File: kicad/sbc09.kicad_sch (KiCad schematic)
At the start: 77 parts, among them J1 Conn_01x03_Male, J2 Conn_01x06_Male, J3 Conn_01x06_Male, J4 Conn_01x06_Male, J5 DB9_Female_MountingHoles, J6 Conn_02x25_Odd_Even, Q1 2N7000, SW1 SW_Push, U1 74LS245, U10 74LS670, U11 74LS670, U12 AS6C4008-55PCN, U13 SST39SF040-DIP, U14 SST39SF040-DIP, U15 XR68C681CJ, U16 MAX232, U2 74LS245, U3 74LS245, U4 MC6809E, U5 74HCT125, U6 ATF22V10C, U7 ATF22V10C, U8 74LS670, U9 74LS670, X1 8MHz, X2 3.6864MHz

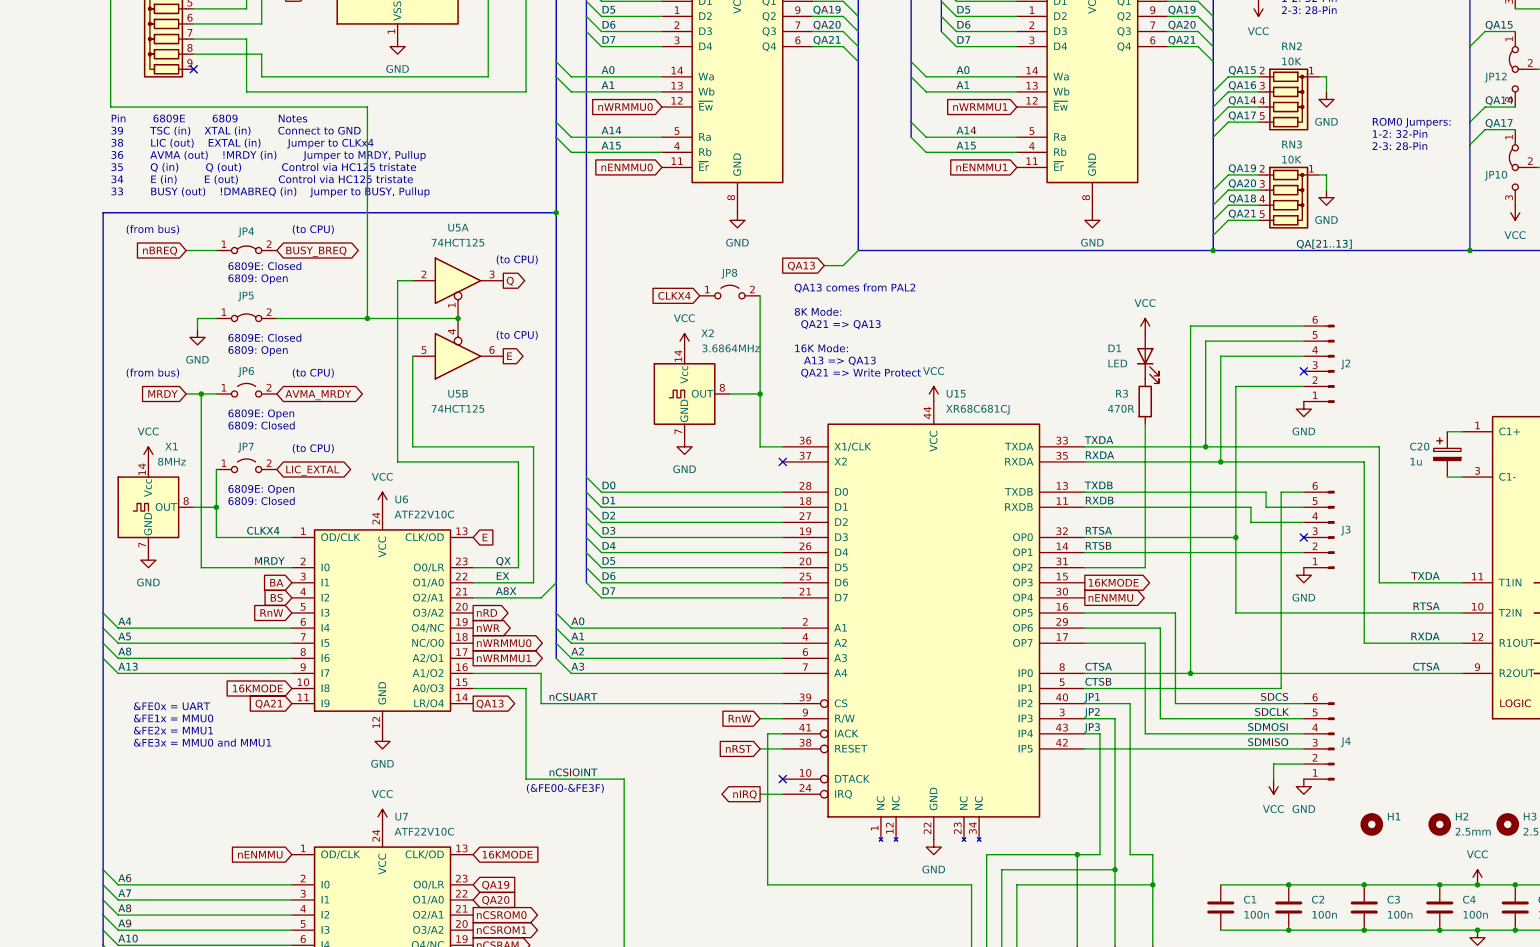
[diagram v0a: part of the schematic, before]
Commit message: Tweak board placement; DIP-8 oscillators
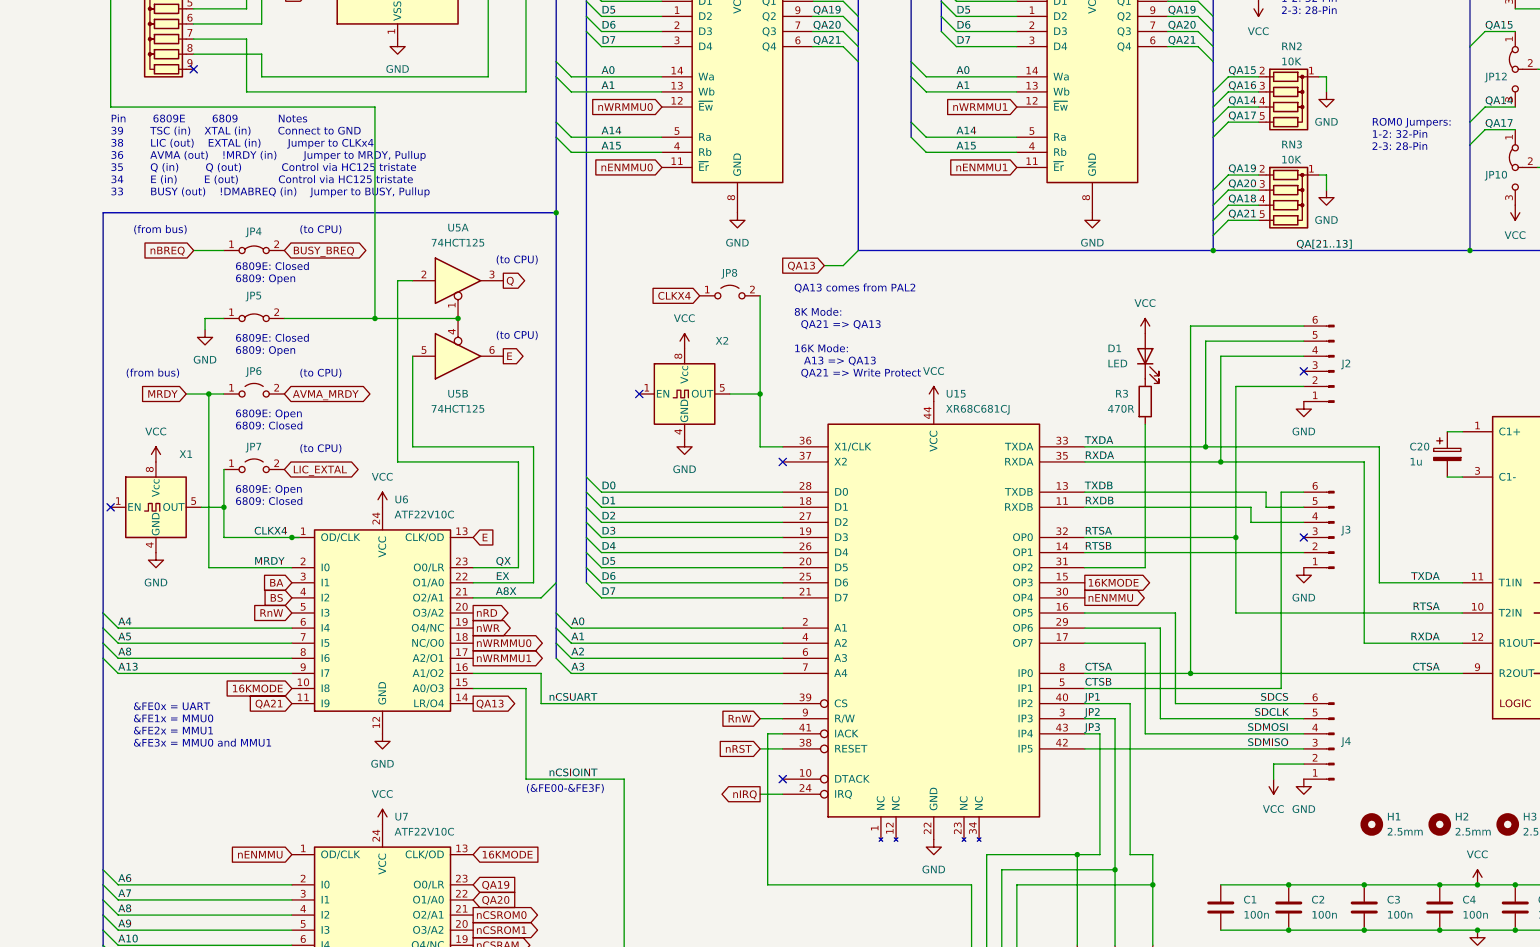
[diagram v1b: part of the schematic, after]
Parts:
- removed X1: 8MHz, Oscillator:Oscillator_DIP-14, symbol Oscillator:ACO-xxxMHz
- removed X2: 3.6864MHz, Oscillator:Oscillator_DIP-14, symbol Oscillator:ACO-xxxMHz
- added X1: (no value), symbol Oscillator:CXO_DIP8
- added X2: (no value), Oscillator:Oscillator_DIP-8, symbol Oscillator:CXO_DIP8
- H1: value (none) -> 2.5mm
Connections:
- net CLKX4: now also X1.5 (OUT)
- net GND: now also X1.4 (GND), X2.4 (GND)
- net VCC: now also X1.8 (Vcc), X2.8 (Vcc)
- net at JP8.2 (B), U15.36 (X1/CLK): now also X2.5 (OUT)
- no-connect marks 14 -> 16
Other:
- moved on the sheet: JP4, JP5, JP6, JP7

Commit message: Minor
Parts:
- J2, J3: footprint Connector_PinSocket_2.54mm:PinSocket_1x06_P2.54mm_Vertical -> (none)
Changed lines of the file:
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@@
       (effects (font (size 1.27 1.27)) (justify right) hide)
     )
-    (property "Footprint" "Connector_PinSocket_2.54mm:PinSocket_1x06_P2.54mm_Vertical" (id 2) (at 222.25 190.5 0)
+    (property "Footprint" "" (id 2) (at 222.25 190.5 0)
       (effects (font (size 1.27 1.27)) hide)
     )
@@
       (effects (font (size 1.27 1.27)) (justify right) hide)
     )
-    (property "Footprint" "Connector_PinSocket_2.54mm:PinSocket_1x06_P2.54mm_Vertical" (id 2) (at 222.25 162.56 0)
-      (effects (font (size 1.27 1.27)) hide)
-    )
+    (property "Footprint" "" (id 2) (at 222.25 162.56 0)
+      (effects (font (size 1.27 1.27)) hide)
+    )

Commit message: Messing with front panel connectors
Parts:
- D1: footprint LED_THT:LED_D3.0mm -> (none)
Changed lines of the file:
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@@
       (effects (font (size 1.27 1.27)) (justify right))
     )
-    (property "Footprint" "LED_THT:LED_D3.0mm" (id 2) (at 190.5 160.02 0)
+    (property "Footprint" "" (id 2) (at 190.5 160.02 0)
       (effects (font (size 1.27 1.27)) hide)
     )
@@
     )
     (path "/fae83aca-d871-4dad-8dca-794c894d9124"
-      (reference "D1") (unit 1) (value "LED") (footprint "LED_THT:LED_D3.0mm")
+      (reference "D1") (unit 1) (value "LED") (footprint "LED_THT:LED_D3.0mm_Horizontal_O1.27mm_Z2.0mm")
     )
     (path "/0fdc7ebb-4b15-4947-a92f-73b17a1787e1"
@@
     )
     (path "/c8679364-5ecf-4ff5-92b0-70a3c93f3773"
-      (reference "J2") (unit 1) (value "Conn_01x06_Male") (footprint "Connector_PinSocket_2.54mm:PinSocket_1x06_P2.54mm_Vertical")
+      (reference "J2") (unit 1) (value "Conn_01x06_Male") (footprint "Connector_PinSocket_2.54mm:PinSocket_1x06_P2.54mm_Horizontal")
     )
     (path "/04d3812c-7a47-4d20-b313-0d4dd0f3856c"
-      (reference "J3") (unit 1) (value "Conn_01x06_Male") (footprint "Connector_PinSocket_2.54mm:PinSocket_1x06_P2.54mm_Vertical")
+      (reference "J3") (unit 1) (value "Conn_01x06_Male") (footprint "Connector_PinSocket_2.54mm:PinSocket_1x06_P2.54mm_Horizontal")
     )
     (path "/acbf984b-95e6-48f0-909b-46f570b1f9ff"

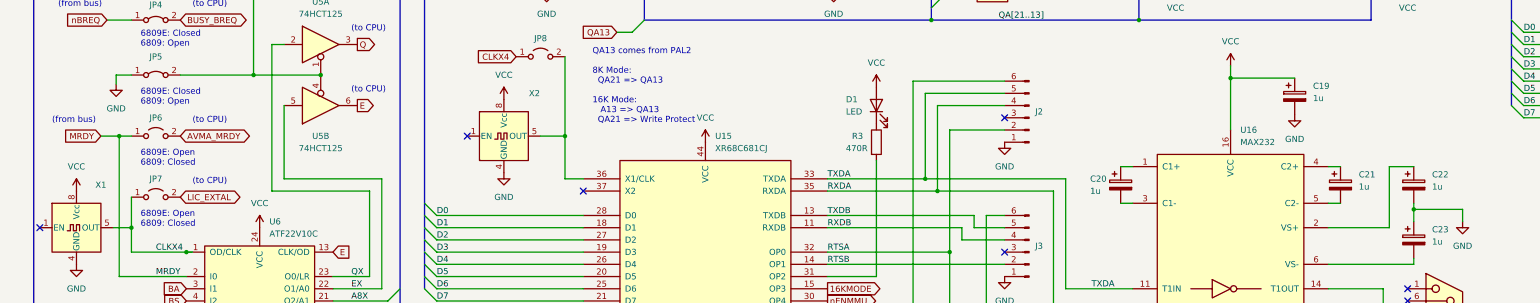
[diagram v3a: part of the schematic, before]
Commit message: OCD tweaking around MAX232E
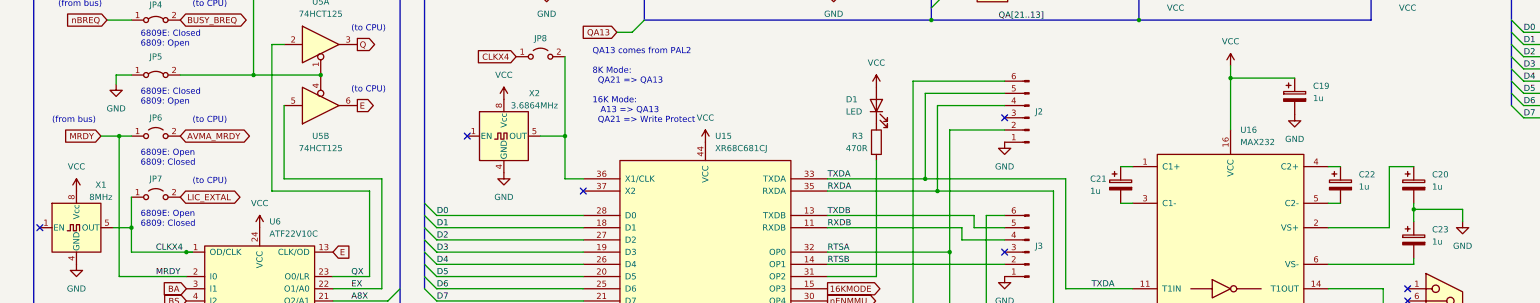
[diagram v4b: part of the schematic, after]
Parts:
- D1: footprint (none) -> LED_THT:LED_D3.0mm_Horizontal_O1.27mm_Z2.0mm
- H1, H2, H3, H4: footprint (none) -> MountingHole:MountingHole_2.7mm
- J2, J3: footprint (none) -> Connector_PinSocket_2.54mm:PinSocket_1x06_P2.54mm_Horizontal
- X1: value (none) -> 8MHz; footprint (none) -> Oscillator:Oscillator_DIP-8
- X2: value (none) -> 3.6864MHz
- renumbered C22 to C20, C20 to C21, C21 to C22
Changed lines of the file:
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@@
       (effects (font (size 1.27 1.27)) (justify right) hide)
     )
-    (property "Footprint" "" (id 2) (at 222.25 190.5 0)
+    (property "Footprint" "Connector_PinSocket_2.54mm:PinSocket_1x06_P2.54mm_Horizontal" (id 2) (at 222.25 190.5 0)
       (effects (font (size 1.27 1.27)) hide)
     )
@@
       (effects (font (size 1.27 1.27)) (justify left))
     )
-    (property "Footprint" "" (id 2) (at 228.6 238.76 0)
+    (property "Footprint" "MountingHole:MountingHole_2.7mm" (id 2) (at 228.6 238.76 0)
       (effects (font (size 1.27 1.27)) hide)
     )
@@
   (symbol (lib_id "Device:C_Polarized") (at 302.26 176.53 0) (unit 1)
     (in_bom yes) (on_board yes)
-    (property "Reference" "C22" (id 0) (at 306.07 174.3709 0)
+    (property "Reference" "C20" (id 0) (at 306.07 174.3709 0)
       (effects (font (size 1.27 1.27)) (justify left))
     )
@@
       (effects (font (size 1.27 1.27)) (justify left))
     )
-    (property "Footprint" "" (id 2) (at 240.03 238.76 0)
+    (property "Footprint" "MountingHole:MountingHole_2.7mm" (id 2) (at 240.03 238.76 0)
       (effects (font (size 1.27 1.27)) hide)
     )
@@
       (effects (font (size 1.27 1.27)) (justify left))
     )
-    (property "Footprint" "" (id 2) (at 251.46 238.76 0)
+    (property "Footprint" "MountingHole:MountingHole_2.7mm" (id 2) (at 251.46 238.76 0)
       (effects (font (size 1.27 1.27)) hide)
     )
@@
     (in_bom yes) (on_board yes)
     (property "Reference" "X1" (id 0) (at 29.21 176.53 0))
-    (property "Value" "" (id 1) (at 29.21 179.07 0))
-    (property "Footprint" "" (id 2) (at 35.56 194.31 0)
+    (property "Value" "8MHz" (id 1) (at 29.21 179.07 0))
+    (property "Footprint" "Oscillator:Oscillator_DIP-8" (id 2) (at 35.56 194.31 0)
       (effects (font (size 1.27 1.27)) hide)
     )
@@
       (effects (font (size 1.27 1.27)) (justify left))
     )
-    (property "Footprint" "" (id 2) (at 262.89 238.76 0)
+    (property "Footprint" "MountingHole:MountingHole_2.7mm" (id 2) (at 262.89 238.76 0)
       (effects (font (size 1.27 1.27)) hide)
     )
@@
   (symbol (lib_id "Device:C_Polarized") (at 287.02 176.53 0) (unit 1)
     (in_bom yes) (on_board yes)
-    (property "Reference" "C21" (id 0) (at 290.83 174.3709 0)
+    (property "Reference" "C22" (id 0) (at 290.83 174.3709 0)
       (effects (font (size 1.27 1.27)) (justify left))
     )
@@
       (effects (font (size 1.27 1.27)) (justify right) hide)
     )
-    (property "Footprint" "" (id 2) (at 222.25 162.56 0)
+    (property "Footprint" "Connector_PinSocket_2.54mm:PinSocket_1x06_P2.54mm_Horizontal" (id 2) (at 222.25 162.56 0)
       (effects (font (size 1.27 1.27)) hide)
     )
@@
   (symbol (lib_id "Device:C_Polarized") (at 241.3 176.53 0) (unit 1)
     (in_bom yes) (on_board yes)
-    (property "Reference" "C20" (id 0) (at 234.95 175.26 0)
+    (property "Reference" "C21" (id 0) (at 234.95 175.26 0)
       (effects (font (size 1.27 1.27)) (justify left))
     )
@@
     (in_bom yes) (on_board yes)
     (property "Reference" "X2" (id 0) (at 119.38 157.48 0))
-    (property "Value" "" (id 1) (at 119.38 160.02 0))
+    (property "Value" "3.6864MHz" (id 1) (at 119.38 160.02 0))
     (property "Footprint" "Oscillator:Oscillator_DIP-8" (id 2) (at 124.46 175.26 0)
       (effects (font (size 1.27 1.27)) hide)
@@
       (effects (font (size 1.27 1.27)) (justify right))
     )
-    (property "Footprint" "" (id 2) (at 190.5 160.02 0)
+    (property "Footprint" "LED_THT:LED_D3.0mm_Horizontal_O1.27mm_Z2.0mm" (id 2) (at 190.5 160.02 0)
       (effects (font (size 1.27 1.27)) hide)
     )
@@
       (reference "C19") (unit 1) (value "1u") (footprint "Capacitor_THT:CP_Radial_D5.0mm_P2.50mm")
     )
-    (path "/d18e651c-7a28-4e43-83aa-1d7e57db7dcb"
+    (path "/308cdfc0-0955-45b8-bde1-e0cd6ea9a51c"
       (reference "C20") (unit 1) (value "1u") (footprint "Capacitor_THT:CP_Radial_D5.0mm_P2.50mm")
     )
-    (path "/b5e3a9b9-beba-4c37-b256-fb994967dbd6"
+    (path "/d18e651c-7a28-4e43-83aa-1d7e57db7dcb"
       (reference "C21") (unit 1) (value "1u") (footprint "Capacitor_THT:CP_Radial_D5.0mm_P2.50mm")
     )
-    (path "/308cdfc0-0955-45b8-bde1-e0cd6ea9a51c"
+    (path "/b5e3a9b9-beba-4c37-b256-fb994967dbd6"
       (reference "C22") (unit 1) (value "1u") (footprint "Capacitor_THT:CP_Radial_D5.0mm_P2.50mm")
     )

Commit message: Moved reset components close to front panel
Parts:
- D1: footprint LED_THT:LED_D3.0mm_Horizontal_O1.27mm_Z2.0mm -> (none)
- SW1: footprint Button_Switch_THT:SW_TH_Tactile_Omron_B3F-10xx -> (none)
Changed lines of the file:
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@@
       (effects (font (size 1.27 1.27)) (justify right) hide)
     )
-    (property "Footprint" "Button_Switch_THT:SW_TH_Tactile_Omron_B3F-10xx" (id 2) (at 12.7 31.75 0)
+    (property "Footprint" "" (id 2) (at 12.7 31.75 0)
       (effects (font (size 1.27 1.27)) hide)
     )
@@
       (effects (font (size 1.27 1.27)) (justify right))
     )
-    (property "Footprint" "LED_THT:LED_D3.0mm_Horizontal_O1.27mm_Z2.0mm" (id 2) (at 190.5 160.02 0)
+    (property "Footprint" "" (id 2) (at 190.5 160.02 0)
       (effects (font (size 1.27 1.27)) hide)
     )
@@
     )
     (path "/fae83aca-d871-4dad-8dca-794c894d9124"
-      (reference "D1") (unit 1) (value "LED") (footprint "LED_THT:LED_D3.0mm_Horizontal_O1.27mm_Z2.0mm")
+      (reference "D1") (unit 1) (value "LED") (footprint "LED_THT:LED_D3.0mm_Horizontal_O6.35mm_Z2.0mm")
     )
     (path "/0fdc7ebb-4b15-4947-a92f-73b17a1787e1"
@@
     )
     (path "/bfcdb47c-dd19-4a95-86c4-e5b0ffd29fe9"
-      (reference "SW1") (unit 1) (value "SW_Push") (footprint "Button_Switch_THT:SW_TH_Tactile_Omron_B3F-10xx")
+      (reference "SW1") (unit 1) (value "SW_Push") (footprint "Button_Switch_THT:SW_Tactile_SPST_Angled_PTS645Vx83-2LFS")
     )
     (path "/b94ab99f-52e3-4ccf-b6fb-e7021a9f054f"

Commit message: Started labelling
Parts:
- D1: footprint (none) -> LED_THT:LED_D3.0mm_Horizontal_O6.35mm_Z2.0mm
- J4: footprint Connector_PinSocket_2.54mm:PinSocket_1x06_P2.54mm_Vertical -> (none)
- SW1: footprint (none) -> Button_Switch_THT:SW_Tactile_SPST_Angled_PTS645Vx83-2LFS
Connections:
- net GND: now also J4.6 (Pin_6); no longer J4.1 (Pin_1)
- net SDCLK: now also J4.2 (Pin_2); no longer J4.5 (Pin_5)
- net SDCS: now also J4.1 (Pin_1); no longer J4.6 (Pin_6)
- net SDMISO: now also J4.4 (Pin_4); no longer J4.3 (Pin_3)
- net SDMOSI: now also J4.3 (Pin_3); no longer J4.4 (Pin_4)
- net VCC: now also J4.5 (Pin_5); no longer J4.2 (Pin_2)
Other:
- moved on the sheet: J4
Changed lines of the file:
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@@
     (pin "9")
   )
-  (symbol (lib_id "Connector:Conn_01x06_Male") (at 222.25 226.06 180) (unit 1)
+  (symbol (lib_id "Connector:Conn_01x06_Male") (at 222.25 223.52 0) (mirror y) (unit 1)
     (in_bom yes) (on_board yes) (fields_autoplaced)
     (property "Reference" "J4" (id 0) (at 223.52 224.7899 0)
       (effects (font (size 1.27 1.27)) (justify right))
     )
-    (property "Value" "Conn_01x06_Male" (id 1) (at 223.52 226.0599 0)
+    (property "Value" "Conn_01x06_Male" (id 1) (at 223.52 223.5201 0)
       (effects (font (size 1.27 1.27)) (justify right) hide)
     )
-    (property "Footprint" "Connector_PinSocket_2.54mm:PinSocket_1x06_P2.54mm_Vertical" (id 2) (at 222.25 226.06 0)
-      (effects (font (size 1.27 1.27)) hide)
-    )
-    (property "Datasheet" "~" (id 3) (at 222.25 226.06 0)
+    (property "Footprint" "" (id 2) (at 222.25 223.52 0)
+      (effects (font (size 1.27 1.27)) hide)
+    )
+    (property "Datasheet" "~" (id 3) (at 222.25 223.52 0)
       (effects (font (size 1.27 1.27)) hide)
     )
@@
       (effects (font (size 1.27 1.27)) (justify right) hide)
     )
-    (property "Footprint" "" (id 2) (at 12.7 31.75 0)
+    (property "Footprint" "Button_Switch_THT:SW_Tactile_SPST_Angled_PTS645Vx83-2LFS" (id 2) (at 12.7 31.75 0)
       (effects (font (size 1.27 1.27)) hide)
     )
@@
       (effects (font (size 1.27 1.27)) (justify right))
     )
-    (property "Footprint" "" (id 2) (at 190.5 160.02 0)
+    (property "Footprint" "LED_THT:LED_D3.0mm_Horizontal_O6.35mm_Z2.0mm" (id 2) (at 190.5 160.02 0)
       (effects (font (size 1.27 1.27)) hide)
     )
@@
     )
     (path "/acbf984b-95e6-48f0-909b-46f570b1f9ff"
-      (reference "J4") (unit 1) (value "Conn_01x06_Male") (footprint "Connector_PinSocket_2.54mm:PinSocket_1x06_P2.54mm_Vertical")
+      (reference "J4") (unit 1) (value "Conn_01x06_Male") (footprint "Connector_PinSocket_2.54mm:PinSocket_1x06_P2.54mm_Horizontal")
     )
     (path "/716fe987-5728-4e91-8766-9b4b10dd1846"
